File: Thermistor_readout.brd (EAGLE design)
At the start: 90 x 60 mm, 25 parts, among them Q1 BC550C, U1 TI_NATIONAL_SEMICONDUCTOR_LF3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, U2 TI_NATIONAL_SEMICONDUCTOR_LF3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, U3 ANALOG_DEVICES_ADG725BSUZANAL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, U4 TI_NATIONAL_SEMICONDUCTOR_LF3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

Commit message: new_connector
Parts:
- removed CON2: (no value), con-harting:CON26L
- added CON1: (no value), con-harting:CON16L
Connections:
- net +15V: now also CON1.12; no longer CON2.22
- net +5V: now also CON1.1; no longer CON2.1
- net -15V: now also CON1.16; no longer CON2.26
- net GND: now also CON1.15; no longer CON2.25
- net N$11: now also CON1.6; no longer CON2.6
- net N$13: now also CON1.2; no longer CON2.2
- net N$14: now also CON1.4; no longer CON2.4
- net N$24: now also CON1.8; no longer CON2.8
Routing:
- net +15V: track 90.3 -> 97.9 mm
- net -15V: track 98.8 -> 91.8 mm
- net +5V: track 88.6 -> 93.1 mm
- net N$11: track 23.2 -> 26.9 mm
- net N$14: track 24.2 -> 27.8 mm
- net N$13: track 25.7 -> 29.2 mm
- net N$24: track 94.4 -> 92.5 mm
- net GND: vias 6 -> 7
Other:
- board text added: "Srylab 02/2022 Thermistors Readout Jacopo De Santis v1.0"
- board text removed: "Srylab 02/2022 Thermistors Readout Jacopo De Santis"

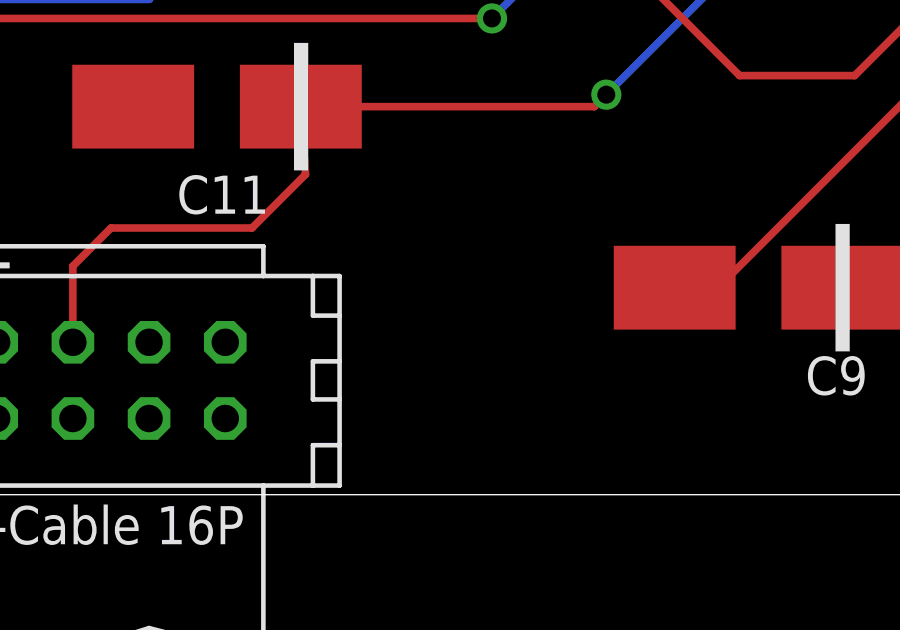
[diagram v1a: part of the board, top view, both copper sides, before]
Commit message: Fix_missing_m15V_connection
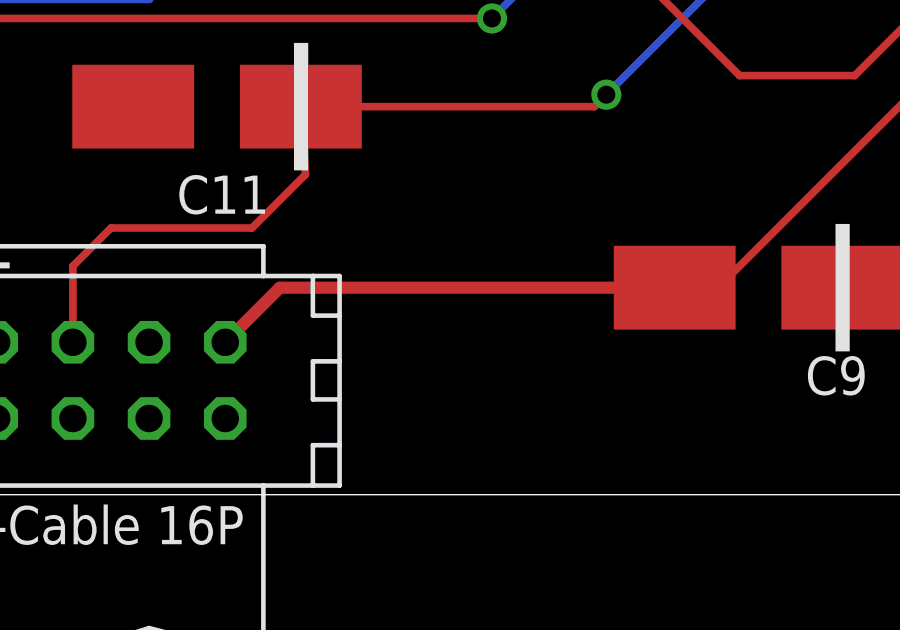
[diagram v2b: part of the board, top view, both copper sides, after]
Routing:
- net -15V: track 91.8 -> 107.6 mm
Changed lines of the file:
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@@
 <wire x1="78.61" y1="17.145" x2="78.675" y2="17.08" width="0.254" layer="1"/>
 <contactref element="CON1" pad="16"/>
-<wire x1="40.005" y1="5.08" x2="54.776" y2="6.69" width="0" layer="19" extent="1-1"/>
+<wire x1="40.005" y1="5.08" x2="41.825" y2="6.9" width="0.4064" layer="1"/>
+<wire x1="41.825" y1="6.9" x2="54.986" y2="6.9" width="0.4064" layer="1"/>
 </signal>
 <signal name="N$4">

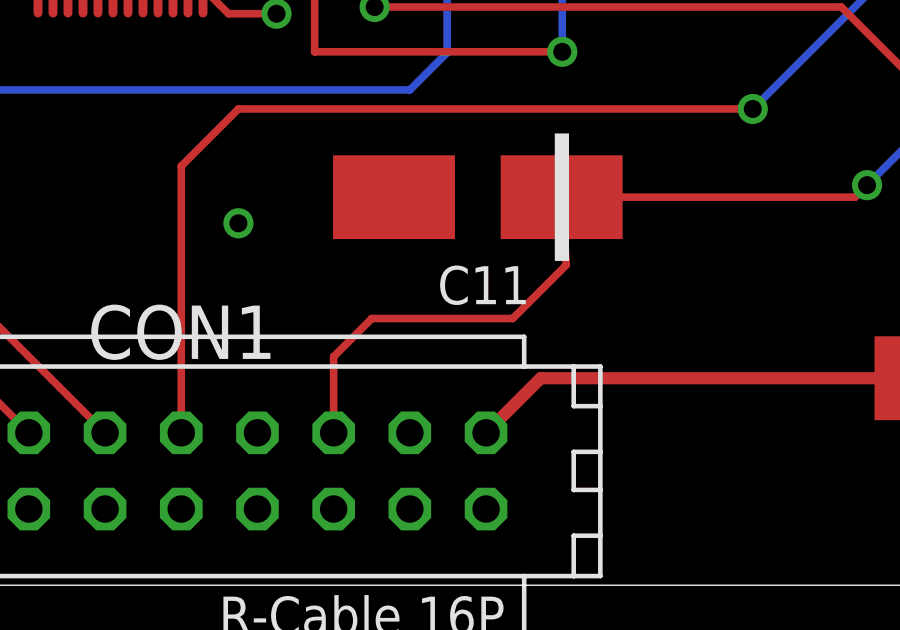
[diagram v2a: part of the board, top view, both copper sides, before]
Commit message: Updated_Flat_cable_connections
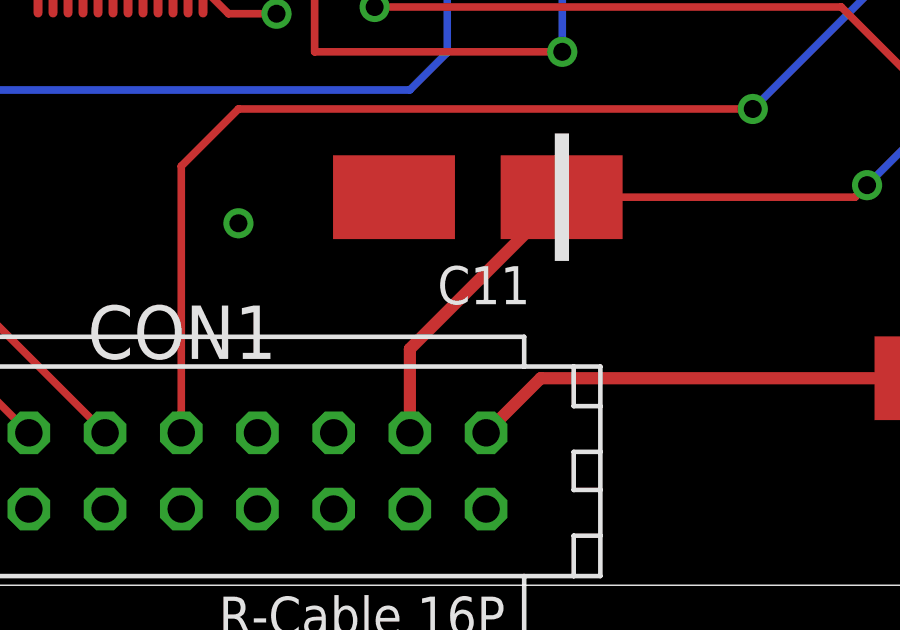
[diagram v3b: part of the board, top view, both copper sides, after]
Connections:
- net +15V: now also CON1.14; no longer CON1.12
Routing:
- net +15V: track 97.9 -> 94.0 mm
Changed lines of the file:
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@@
 <contactref element="U4" pad="7"/>
 <contactref element="C11" pad="1"/>
-<wire x1="42.68" y1="10.674" x2="42.524" y2="12.935" width="0.254" layer="1"/>
 <wire x1="62.495" y1="47.565" x2="62.495" y2="50.512" width="0.254" layer="1"/>
 <wire x1="62.495" y1="50.512" x2="62.58" y2="50.597" width="0.254" layer="1"/>
@@
 <wire x1="78.74" y1="34.29" x2="78.74" y2="33.14" width="0.254" layer="1"/>
 <wire x1="78.74" y1="33.14" x2="78.645" y2="33.045" width="0.254" layer="1"/>
-<contactref element="CON1" pad="12"/>
-<wire x1="34.925" y1="5.08" x2="34.925" y2="7.62" width="0.254" layer="1"/>
-<wire x1="34.925" y1="7.62" x2="36.195" y2="8.89" width="0.254" layer="1"/>
-<wire x1="36.195" y1="8.89" x2="40.896" y2="8.89" width="0.254" layer="1"/>
-<wire x1="40.896" y1="8.89" x2="42.68" y2="10.674" width="0.254" layer="1"/>
+<contactref element="CON1" pad="14"/>
+<wire x1="42.524" y1="12.935" x2="37.465" y2="7.876" width="0.4064" layer="1"/>
+<wire x1="37.465" y1="7.876" x2="37.465" y2="5.08" width="0.4064" layer="1"/>
 </signal>
 <signal name="-15V">
